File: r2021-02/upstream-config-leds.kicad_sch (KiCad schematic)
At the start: 60 parts, among them J1 Conn_01x03_Male, J2 USB_A male UP, J3 USB_B_Micro (up), U1 2k i2c eeprom, U2 NUP4202, U3 USB2517, Y1 24MHz

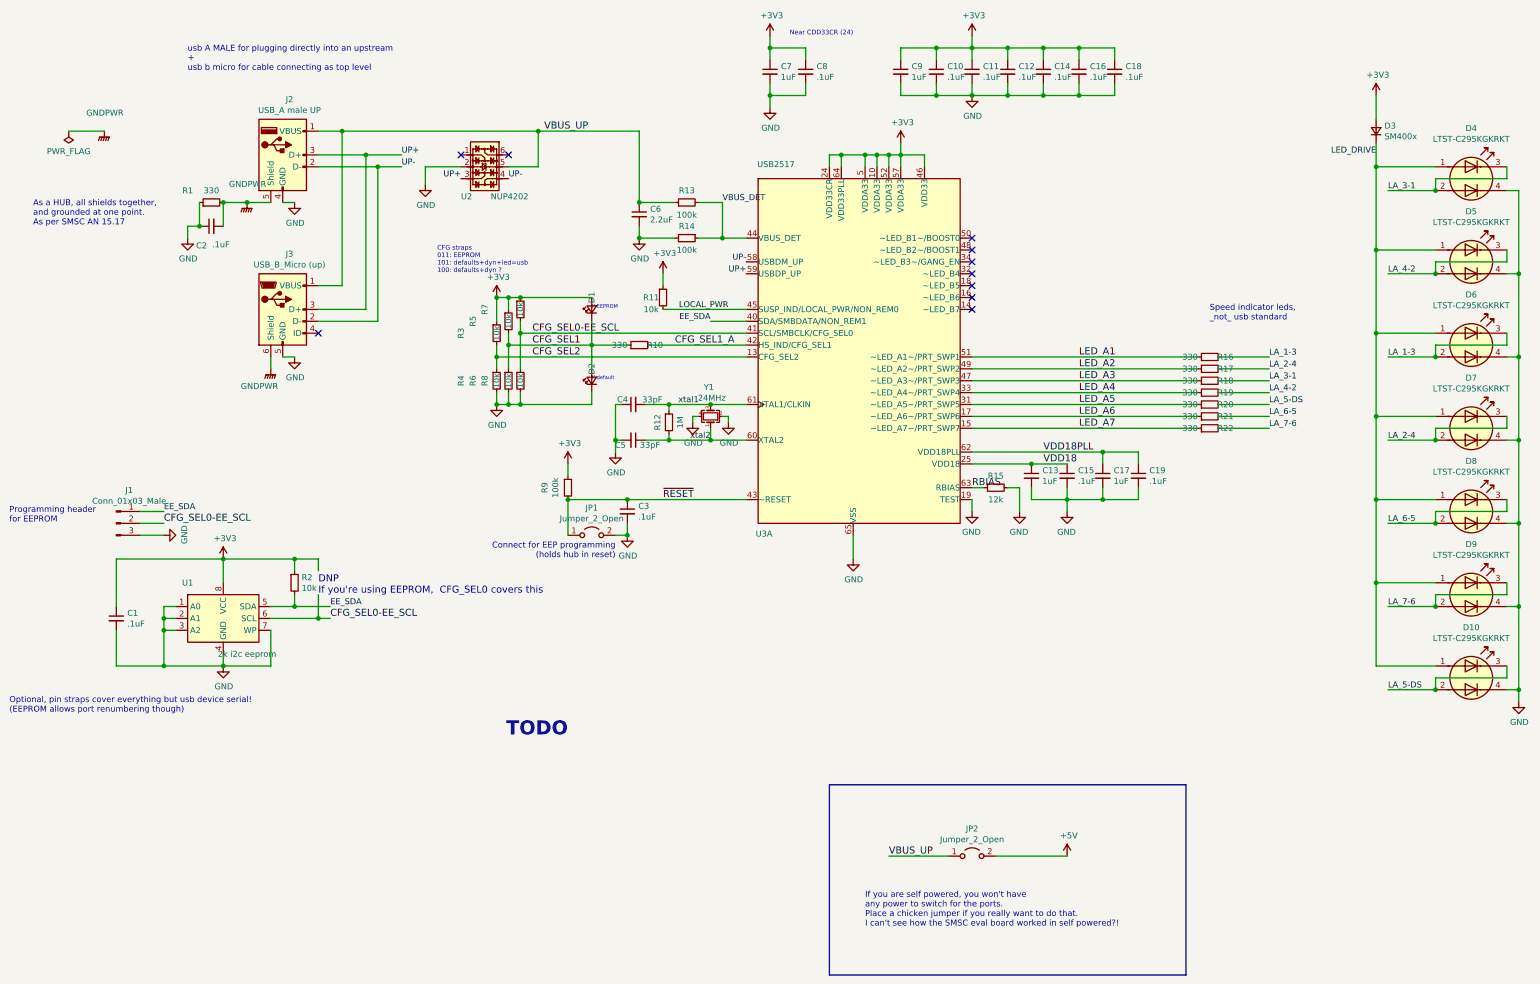
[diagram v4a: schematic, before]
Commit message: BOM revisions for a rev3
Probably not going to bother even assembling rev2 pcbs.  Was missing
parts, found other things that were a little non-ideal.

Decided to start revising towards making it assembleable by JLC, so
using super cheap parts from their basic line where possible, and
minimizing bom items.
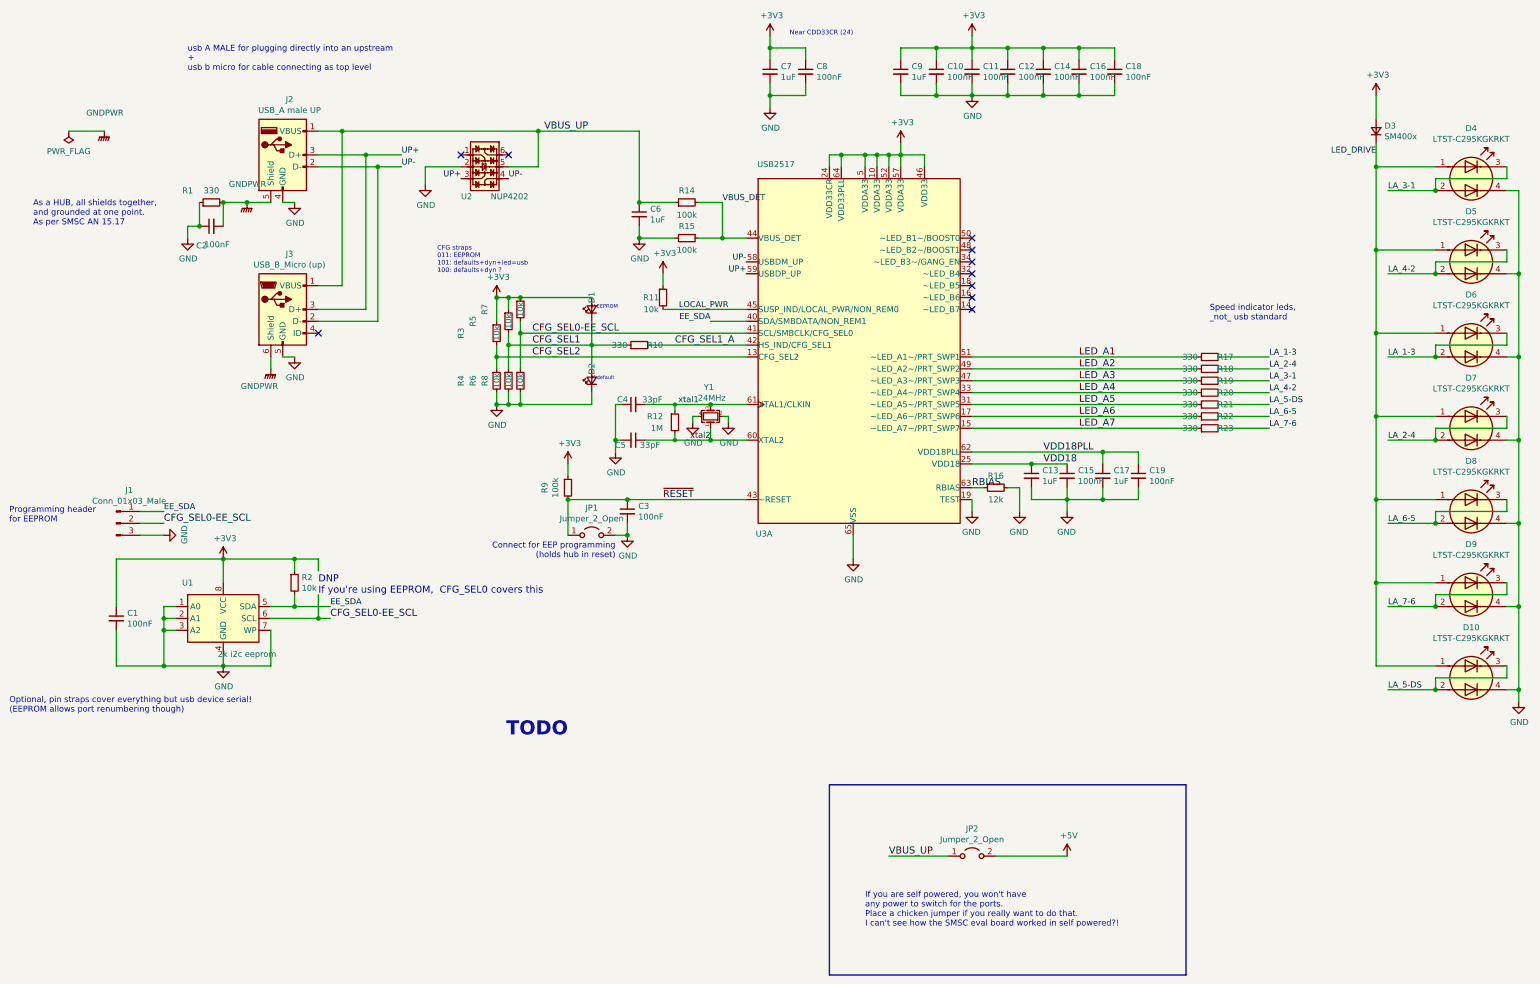
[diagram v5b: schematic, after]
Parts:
- C1, C10, C11, C12, C14, C15, C16, C18, C19, C2, C3, C8: value .1uF -> 100nF; MPN (none) -> CC0603KRX7R9BB104; jlc-basic (none) -> 1; lcsc# (none) -> C14663
- C13, C17, C7, C9: MPN (none) -> CL10A105KB8NNNC; jlc-basic (none) -> 1; lcsc# (none) -> C15849
- C4, C5: MPN (none) -> CL10C330JB8NNNC; jlc-basic (none) -> 1; lcsc# (none) -> C1663
- C6: value 2.2uF -> 1uF; MPN (none) -> CL10A105KB8NNNC; jlc-basic (none) -> 1; lcsc# (none) -> C15849
- R1, R10: MPN (none) -> 0603WAF3300T5E; jlc-basic (none) -> 1; lcsc# (none) -> C23138
- R11, R2, R3, R4, R5, R6, R7, R8: MPN (none) -> 0603WAF1002T5E; jlc-basic (none) -> 1; lcsc# (none) -> C25804
- R12: MPN (none) -> 0603WAF1004T5E; jlc-basic (none) -> 1; lcsc# (none) -> C22935
- R14: renamed from R13; MPN (none) -> 0603WAF1003T5E; jlc-basic (none) -> 1; lcsc# (none) -> C25803
- R15: renamed from R14; MPN (none) -> 0603WAF1003T5E; jlc-basic (none) -> 1; lcsc# (none) -> C25803
- R16: renamed from R15; MPN (none) -> 0603WAF1202T5E; jlc-basic (none) -> 1; lcsc# (none) -> C22790
- R17: renamed from R16; MPN (none) -> 0603WAF3300T5E; jlc-basic (none) -> 1; lcsc# (none) -> C23138
- R18: renamed from R17; MPN (none) -> 0603WAF3300T5E; jlc-basic (none) -> 1; lcsc# (none) -> C23138
- R19: renamed from R18; MPN (none) -> 0603WAF3300T5E; jlc-basic (none) -> 1; lcsc# (none) -> C23138
- R20: renamed from R19; MPN (none) -> 0603WAF3300T5E; jlc-basic (none) -> 1; lcsc# (none) -> C23138
- R21: renamed from R20; MPN (none) -> 0603WAF3300T5E; jlc-basic (none) -> 1; lcsc# (none) -> C23138
- R22: renamed from R21; MPN (none) -> 0603WAF3300T5E; jlc-basic (none) -> 1; lcsc# (none) -> C23138
- R23: renamed from R22; MPN (none) -> 0603WAF3300T5E; jlc-basic (none) -> 1; lcsc# (none) -> C23138
- R9: MPN (none) -> 0603WAF1003T5E; jlc-basic (none) -> 1; lcsc# (none) -> C25803
- U1: MPN FT24C02A -> M24C02-WMN6TP; jlc-basic (none) -> 1; lcsc# (none) -> C7562
- U2: footprint Package_TO_SOT_SMD:SOT-363_SC-70-6 -> Package_TO_SOT_SMD:SOT-23-6; MPN (none) -> SRV05-4-P-T7; jlc-basic (none) -> 1; lcsc# (none) -> C85364
- U3: MPN (none) -> USB2517I-JZX-TR; jlc-basic (none) -> 0; lcsc# (none) -> C626667
- Y1: MPN (none) -> CF4024M00012T8188046; jlc-basic (none) -> 0; lcsc# (none) -> C709021
